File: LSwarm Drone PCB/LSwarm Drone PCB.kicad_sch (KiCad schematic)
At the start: 128 parts, among them J1 Conn_01x04_Pin, J3 JST / BT2.0 Connector, J4 Conn_01x02_Pin, J5 Conn_01x02_Pin, J6 Conn_01x02_Pin, J7 Conn_01x02_Pin, Q1 AO3400A, Q2 AO3400A, Q3 AO3400A, Q4 AO3400A, Q7 AO3407A, SW1 MSK12C02, SW2 SKRPACE010, SW3 SKRPACE010, SW4 SKRPACE010, SW5 SKRPACE010, U1 LSM6DSRTR, U12 AP2112K-3.3, U3 TPS61023DRLR, U4 SN74LVC1T45DBVR, U5 BMP581, X1 X322512MSB4SI

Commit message: sync
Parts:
- added D5: USBLC6-2SC6_C2687116, easyeda2kicad:SOT-23-6_L2.9-W1.6-P0.95-LS2.8-BL, symbol easyeda2kicad:USBLC6-2SC6_C2687116
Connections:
- net GND: now also D5.2 (GND)
- net at USB1.A6 (DP1), USB1.B6 (DP2): now also D5.6 (I/O1); no longer R35.2
- net at USB1.A7 (DN1), USB1.B7 (DN2): now also D5.1 (I/O1); no longer R34.1
- net at USB1.A4 (VBUS), USB1.A9 (VBUS), USB1.B4 (VBUS)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: now also D5.5 (VBUS)
- new net: D5.3 (I/O2), R34.1
- new net: D5.4 (I/O2), R35.2
- no-connect marks 31 -> 30
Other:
- moved on the sheet: R34, R35

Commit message: sync
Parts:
- removed J1: Conn_01x04_Pin, Connector_PinHeader_2.54mm:PinHeader_1x04_P2.54mm_Vertical, symbol Connector:Conn_01x04_Pin
- added J2: Conn_01x06_Pin, Connector_PinHeader_2.54mm:PinHeader_1x06_P2.54mm_Vertical, symbol Connector:Conn_01x06_Pin
- added J8: Conn_01x05_Pin, Connector_PinHeader_2.54mm:PinHeader_1x05_P2.54mm_Vertical, symbol Connector:Conn_01x05_Pin
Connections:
- net +3.3V: now also J2.5 (Pin_5), J8.1 (Pin_1)
- net GND: now also J2.6 (Pin_6), J8.2 (Pin_2)
- net RP2350_GPIO_14: now also J2.3 (Pin_3)
- net RP2350_GPIO_15: now also J2.4 (Pin_4)
- net RP2350_GPIO_16: now also J2.2 (Pin_2)
- net RP2350_GPIO_17: now also J2.1 (Pin_1)
- net RP2350_SWCLK: now also J8.3 (Pin_3)
- net RP2350_SWDIO: now also J8.4 (Pin_4)
- net USB_D-: now reaches D5.1 (I/O1), USB1.A7 (DN1), USB1.B7 (DN2)
- net USB_D+: now reaches D5.6 (I/O1), USB1.A6 (DP1), USB1.B6 (DP2)
- net RP2350_RUN: now reaches C9.1, RP2350.26 (RUN), SW2.1
- net RP2350_RUN: now also J8.5 (Pin_5)
- net RP2350_USB_DM renamed RP2350_USB_DN
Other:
- note added: "ESP32-C3 DEBUG"
- moved on the sheet: C10, C11, C12, C13

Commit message: sync
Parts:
- removed C26: 10nF, Capacitor_SMD:C_0603_1608Metric, symbol Device:C
- removed D5: USBLC6-2SC6_C2687116, easyeda2kicad:SOT-23-6_L2.9-W1.6-P0.95-LS2.8-BL, symbol easyeda2kicad:USBLC6-2SC6_C2687116
- removed R32, R33: 5.1k, Resistor_SMD:R_0603_1608Metric, symbol Device:R
- removed R34, R35: 27, Resistor_SMD:R_0603_1608Metric, symbol Device:R
- removed USB1: USB-TYPE-C-018, easyeda2kicad:USB-C_SMD-TYPE-C-31-M-12, symbol easyeda2kicad:USB-TYPE-C-018
- added C27: 10nF, Capacitor_SMD:C_0603_1608Metric, symbol Device:C
- added D6: USBLC6-2SC6_C2687116, easyeda2kicad:SOT-23-6_L2.9-W1.6-P0.95-LS2.8-BL, symbol easyeda2kicad:USBLC6-2SC6_C2687116
- added R38, R41: 5.1k, Resistor_SMD:R_0603_1608Metric, symbol Device:R
- added R39, R40: 27, Resistor_SMD:R_0603_1608Metric, symbol Device:R
- added USB2: USB-TYPE-C-018, easyeda2kicad:USB-C_SMD-TYPE-C-31-M-12, symbol easyeda2kicad:USB-TYPE-C-018
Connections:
- net GND: now also C27.1, D6.2 (GND), R38.1, R41.2, USB2.A1 (GND), USB2.A12 (GND), USB2.B1 (GND), USB2.B12 (GND)
- net RP2350_USB_DN: now also R40.2
- net RP2350_USB_DP: now also R39.1
- net USB_D+: now also D6.3 (I/O2), USB2.A6 (DP1), USB2.B6 (DP2)
- net USB_D-: now also D6.1 (I/O1), USB2.A7 (DN1), USB2.B7 (DN2)
- new net: D6.6 (I/O1), R40.1
- new net: D6.4 (I/O2), R39.2
- new net: R41.1, USB2.A5 (CC1)
- new net: R38.2, USB2.B5 (CC2)
- new net: C27.2, USB2.0 (SH), USB2.1 (SH), USB2.2 (SH), USB2.3 (SH)
- new net USB_VBUS: D6.5 (VBUS), USB2.A4 (VBUS), USB2.A9 (VBUS), USB2.B4 (VBUS), USB2.B9 (VBUS)
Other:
- note added: "ESD Protection"
- moved on the sheet: C10, C11, C12, C13, C14, C15, C16, C17, C18, C19, C20, C21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

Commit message: finished new pcb wiring
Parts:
- removed C49, C50, C51, C53, C56, C57, C58: 100nF, Capacitor_SMD:C_0603_1608Metric, symbol Device:C
- removed C54: 10nF, Capacitor_SMD:C_0603_1608Metric, symbol Device:C
- removed C59: 1uF, Capacitor_SMD:C_0603_1608Metric, symbol Device:C
- removed C60, C61: 3.3pF, Capacitor_SMD:C_0603_1608Metric, symbol Device:C
- removed ESP32: ESP32-C3, Package_DFN_QFN:QFN-32-1EP_5x5mm_P0.5mm_EP3.7x3.7mm, symbol MCU_Espressif:ESP32-C3
- removed JP1: U.FL-R-SMT-1, easyeda2kicad:RF-SMD_FRF05002-JSS103M, symbol easyeda2kicad:U.FL-R-SMT-1
- removed L7: 2nH, Inductor_SMD:L_0402_1005Metric, symbol Device:L
- removed L8: 2.2nH, Inductor_SMD:L_0402_1005Metric, symbol Device:L
- removed R14, R15, R16: 10k, Resistor_SMD:R_0603_1608Metric, symbol Device:R
- removed SW4, SW5: SKRPACE010, easyeda2kicad:KEY-SMD_4P-L4.2-W3.2-P2.20-LS4.6, symbol easyeda2kicad:SKRPACE010
- added C52: 1uF, Capacitor_SMD:C_0603_1608Metric, symbol Device:C
- added C55: 10uF, Capacitor_SMD:C_0603_1608Metric, symbol Device:C
- added R18, R32, R33: 10k, Resistor_SMD:R_0603_1608Metric, symbol Device:R
- added U6: ESP32-C3-MINI-1U-N4, easyeda2kicad:WIFIM-SMD_61P-L13.2-W12.5-P0.80, symbol easyeda2kicad:ESP32-C3-MINI-1U-N4
- C7, C8: value 15pF -> 33pF
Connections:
- net +3.3V: now also C55.2, R18.2, R32.1, R33.1
- net GND: now also C8.2, C52.1, U6.1 (GND), U6.11 (GND), U6.14 (GND), U6.2 (GND), U6.36 (GND), U6.37 (GND), U6.38 (GND), U6.39 (GND), U6.40 (GND), U6.41 (GND), U6.42 (GND), U6.43 (GND), U6.44 (GND), U6.45 (GND), U6.46 (GND), U6.47 (GND), U6.48 (GND), U6.49 (GND), U6.50 (GND), U6.51 (GND), U6.52 (GND), U6.53 (GND), U6.54 (GND), U6.55 (GND), U6.56 (GND), U6.57 (GND), U6.58 (GND), U6.59 (GND), U6.60 (GND), U6.61 (GND); no longer C8.1
- net RP2350_GPIO_0: now also U6.30 (RXD0)
- net RP2350_GPIO_1: now also U6.31 (TXD0)
- net RP2350_GPIO_14: no longer RP2350.18 (GPIO14)
- net RP2350_GPIO_15: no longer RP2350.19 (GPIO15)
- net RP2350_GPIO_16: no longer RP2350.27 (GPIO16)
- net RP2350_GPIO_17: no longer RP2350.28 (GPIO17)
- net RP2350_GPIO_2: now also C52.2, R18.1, U6.8 (EN)
- net RP2350_GPIO_25_5.5V: now also R19.1; no longer R19.2
- net RP2350_GPIO_3: now also U6.23 (IO9)
- net RP2350_XIN: now also C8.1; no longer C8.2
- net RP2350_XOUT: now also R7.1; no longer R7.2
- net at U4.4 (B): now also R19.2; no longer R19.1
- net at C7.2, X1.3 (OSC2): now also R7.2; no longer R7.1
- net RP2350_GPIO_12: no longer names the net of RP2350.16 (GPIO12)
- net RP2350_GPIO_13: no longer names the net of RP2350.17 (GPIO13)
- net RP2350_GPIO_23: no longer names the net of RP2350.35 (GPIO23)
- net RP2350_GPIO_27_ADC: no longer names the net of RP2350.41 (GPIO27/ADC1)
- net RP2350_GPIO_28_ADC: no longer names the net of RP2350.42 (GPIO28/ADC2)
- net RP2350_GPIO_29_ADC: no longer names the net of RP2350.43 (GPIO29/ADC3)
- new net: R33.2, U6.22 (IO8)
- new net: R32.2, U6.5 (IO2)
- new net: C55.1, U6.3 (3V3)
- no-connect marks 30 -> 45
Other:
- note added: "RX"
- note added: "TX"
- note removed: "ESP32 BOOT"
- note removed: "ESP32 EN"
- note removed: "ESP32 VDD"
- note removed: "ESP32-C3"
- note removed: "Near VDD & VDDA Pins"
- note removed: "Near VDD_3P3"
- moved on the sheet: BUZZER2, C1, C27, C48, C71, C71Ceramic1, C8, D6, J2, Q7, R17, R19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

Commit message: sync
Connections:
- net RP2350_GPIO_14 is gone; now on net RP2350_GPIO_2: J2.3 (Pin_3)
- net RP2350_GPIO_15 is gone; now on net RP2350_GPIO_3: J2.4 (Pin_4)
- net RP2350_GPIO_16 is gone; now on net RP2350_GPIO_1: J2.2 (Pin_2)
- net RP2350_GPIO_17 is gone; now on net RP2350_GPIO_0: J2.1 (Pin_1)

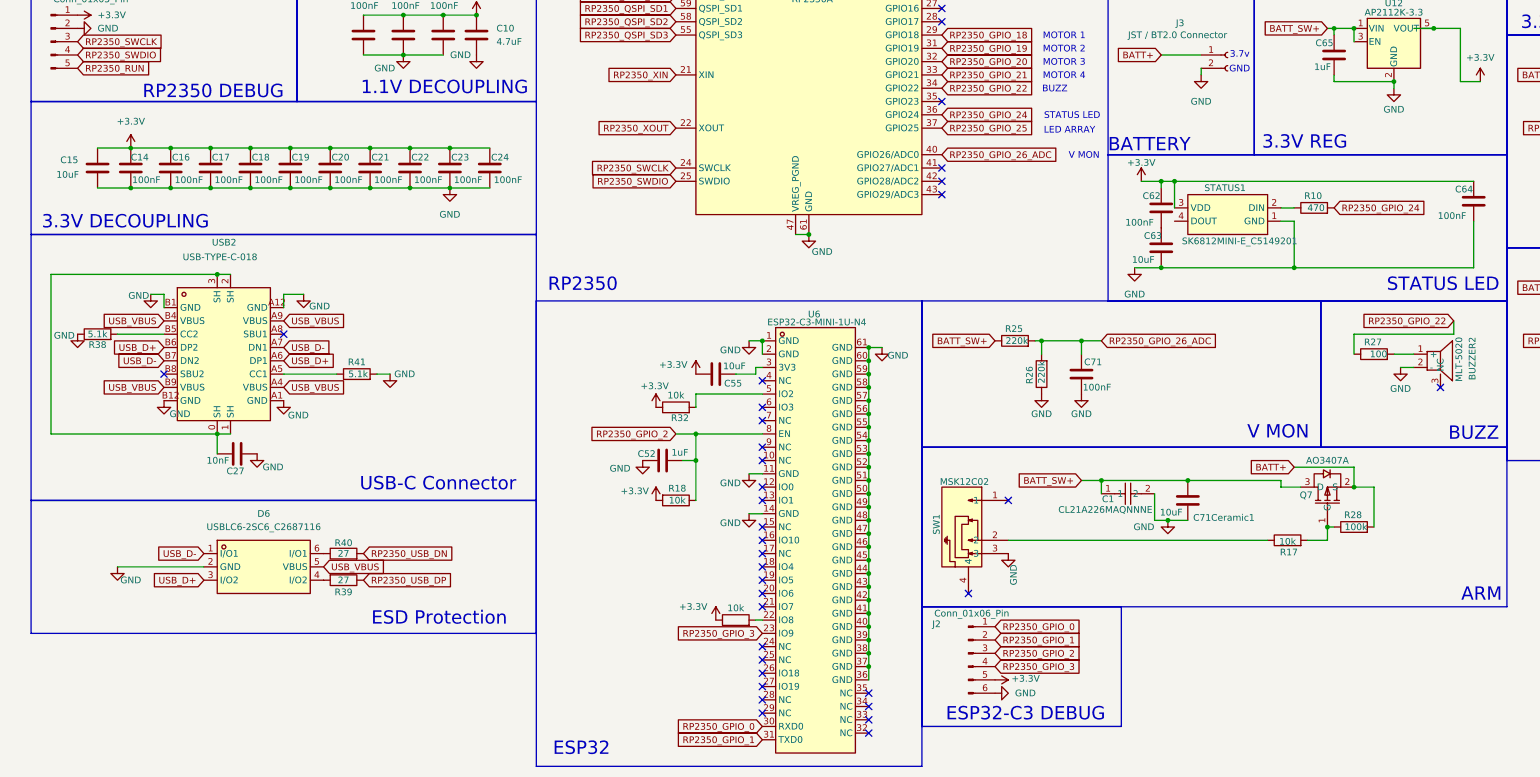
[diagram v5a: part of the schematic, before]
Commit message: added vbus connection to rp2350
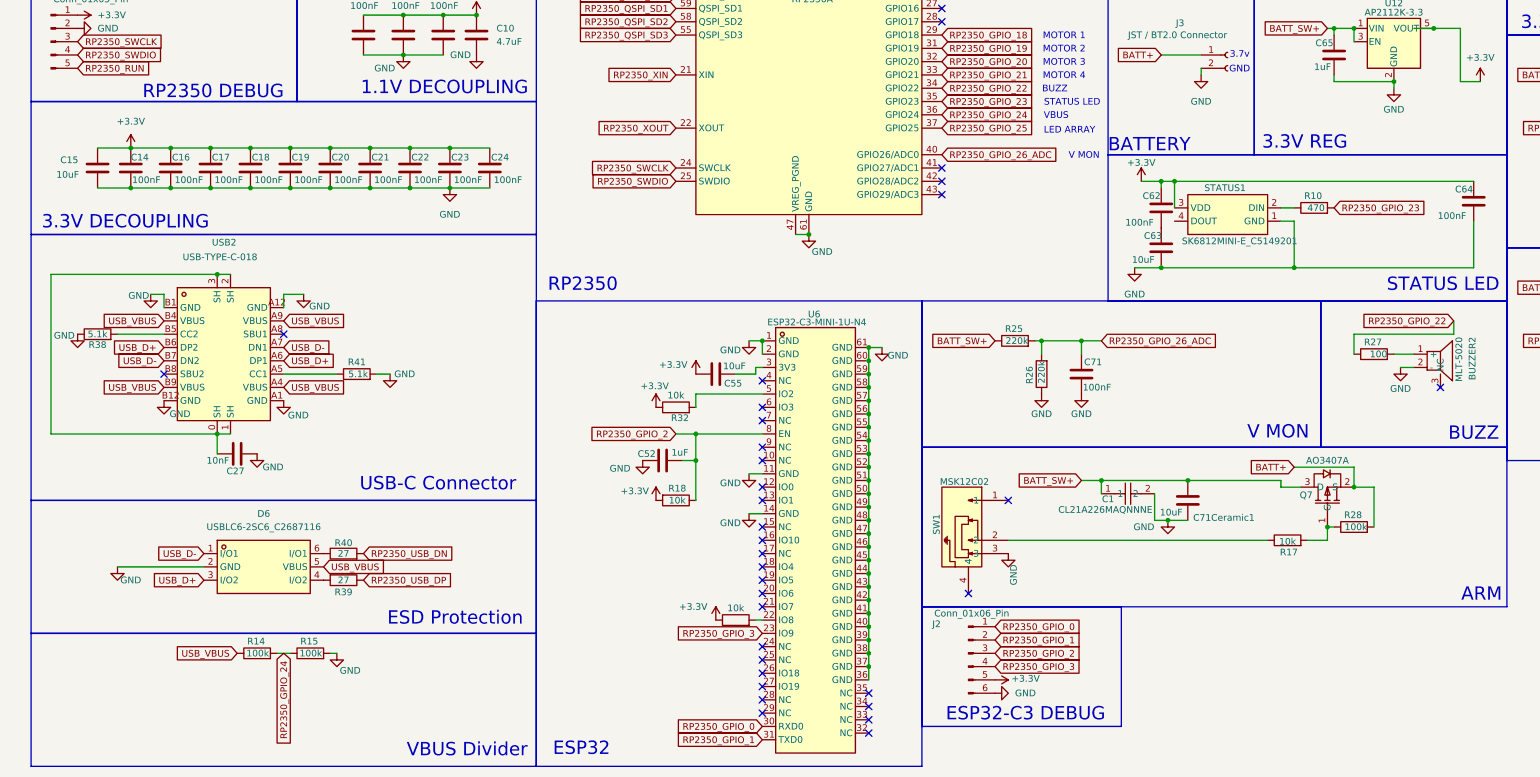
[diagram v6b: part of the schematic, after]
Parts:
- added R14, R15: 100k, Resistor_SMD:R_0603_1608Metric, symbol Device:R
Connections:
- net GND: now also R15.2
- net RP2350_GPIO_24: now also R14.2, R15.1; no longer R10.2
- net USB_VBUS: now also R14.1
- net RP2350_GPIO_23: now reaches RP2350.35 (GPIO23)
- net RP2350_GPIO_23: now also R10.2
- no-connect marks 45 -> 44
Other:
- note added: "VBUS"
- note added: "VBUS Divider"
